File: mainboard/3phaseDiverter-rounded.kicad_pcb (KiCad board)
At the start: 2 copper layers, 133.8 x 119.3 mm, 138 parts, among them CN1 SMA, IC1 ATmega328-P, IC2 LM358, J0 FTDI, J1 RESET, J10 D10, J11 D11, J12 D12, J13 D13, J16 D2, J17 D3, J18 D4, J19 D5, J2 D2, J21 D6, J22 D7, J23 D8, J24 D9, J25 D10, J26 D11, J27 D12, J28 D13, J3 D3, J30 OLED, J31 DS18B20, J32 DS18B20, J4 D4, J5 D5, J6 D6, J7 D7, J8 D8, J9 D9, U1 AP2112R5-3.3TRG1, X1 16MHz

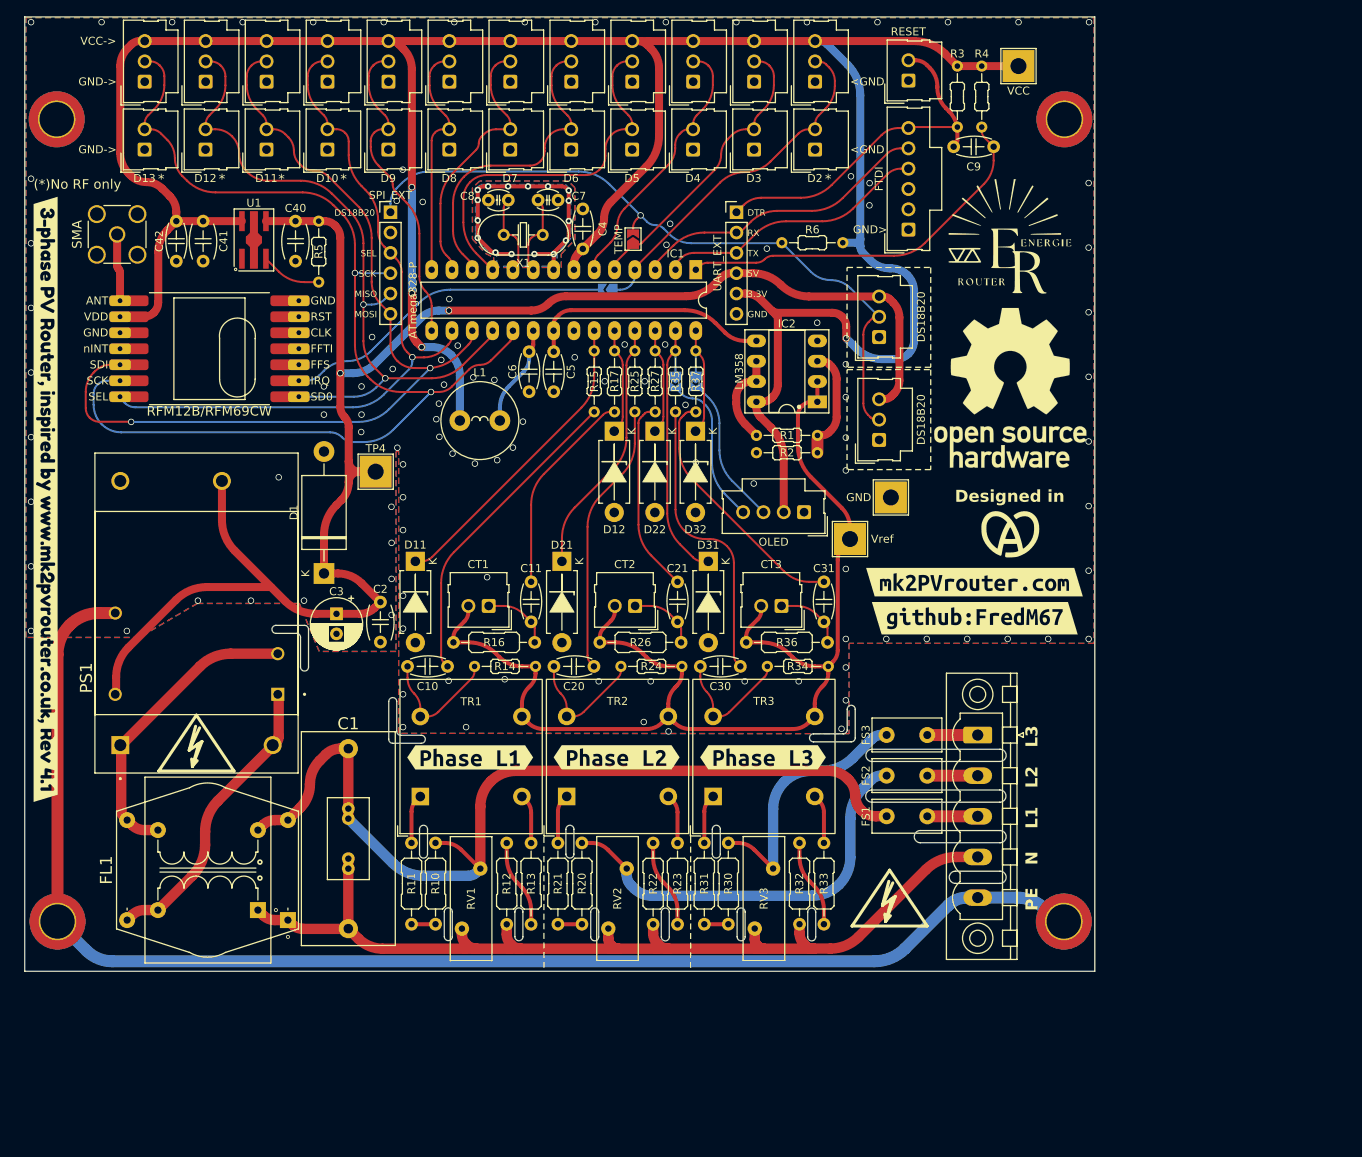
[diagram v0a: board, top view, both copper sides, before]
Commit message: Some SMD components
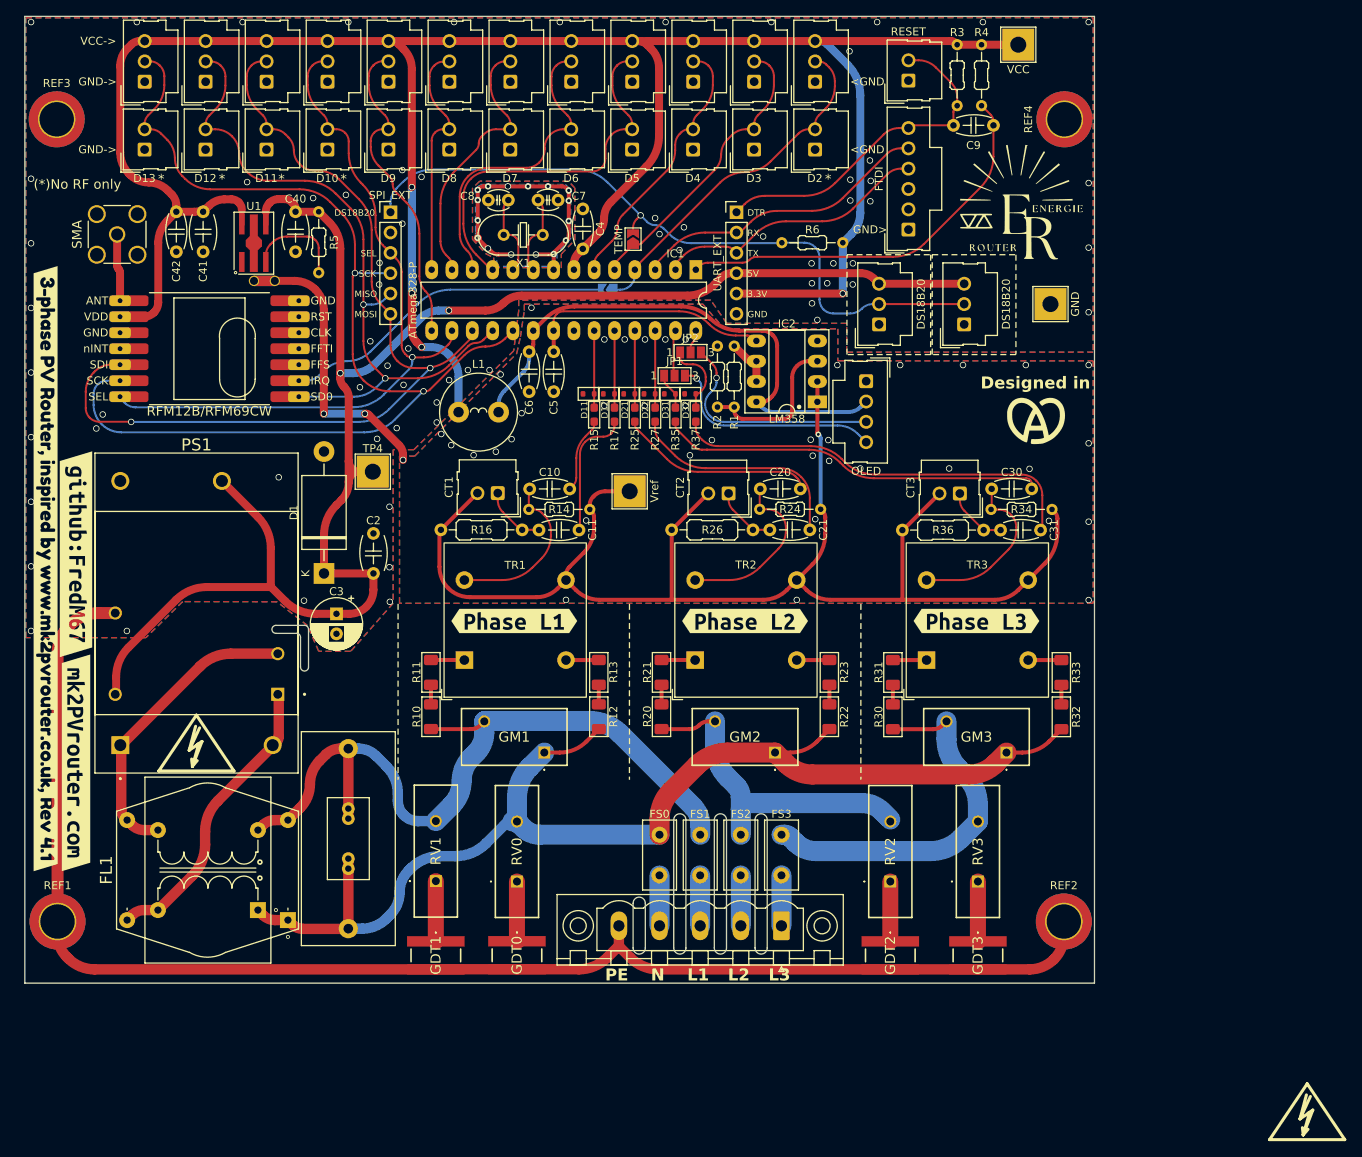
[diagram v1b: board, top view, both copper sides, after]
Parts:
- removed REF**: OSHW-Logo_19x20mm_SilkScreen, Symbol:OSHW-Logo_19x20mm_SilkScreen
- added FS0: 1A x 250V, Fuse:Fuse_Littelfuse_395Series, F.Cu at (92.6, 118.9)
- added GDT0: 2093-300-SM-RPLF, UserDef:2093300SMRPLF, F.Cu at (74.8, 134.0)
- added GDT1: 2093-300-SM-RPLF, UserDef:2093300SMRPLF, F.Cu at (64.6, 134.0)
- added GDT2: 2093-300-SM-RPLF, UserDef:2093300SMRPLF, F.Cu at (121.5, 134.0)
- added GDT3: 2093-300-SM-RPLF, UserDef:2093300SMRPLF, F.Cu at (132.4, 134.0)
- added GM1: 320V, UserDef:IsoM3300BL5, F.Cu at (78.2, 108.7)
- added GM2: 320V, UserDef:IsoM3300BL5, F.Cu at (107.0, 108.7)
- added GM3: 320V, UserDef:IsoM3300BL5, F.Cu at (136.0, 108.7)
- added NT0: NetTie_2, NetTie:NetTie-2_THT_Pad1.0mm, F.Cu at (41.9, 49.7)
- added RV0: 300V, UserDef:MOV14D471KKTR, F.Cu at (74.8, 124.8)
- D11, D12, D21, D22, D31, D32: value SA5.0A-TP -> UCLAMP3301H.TCT; footprint PCM_Diode_THT_AKL:D_DO-15_P10.16mm_Horizontal_Zener -> PCM_Diode_SMD_Handsoldering_AKL:D_SOD-523_TVS
- JP1, JP2: value SolderJumper_2_Open -> SolderJumper_3_Open; footprint Jumper:SolderJumper-2_P1.3mm_Open_TrianglePad1.0x1.5mm -> Jumper:SolderJumper-3_P1.3mm_Open_Pad1.0x1.5mm_NumberLabels; moved to F.Cu
- R10, R11, R12, R13, R20, R21, R22, R23, R30, R31, R32, R33: footprint PCM_Resistor_THT_AKL:R_Axial_DIN0207_L6.3mm_D2.5mm_P10.16mm_Horizontal -> PCM_Resistor_SMD_AKL:R_1206_3216Metric_Pad1.30x1.75mm_HandSolder
- R15, R17, R25, R27, R35, R37: footprint PCM_Resistor_THT_AKL:R_Axial_DIN0204_L3.6mm_D1.6mm_P7.62mm_Horizontal -> PCM_Resistor_SMD_AKL:R_0603_1608Metric_Pad1.05x0.95mm_HandSolder
- RV1, RV2, RV3: value Varistor -> 300V; footprint Varistor:RV_Disc_D15.5mm_W5.2mm_P7.5mm -> UserDef:MOV14D471KKTR
- moved kibuzzard-6431D11C-1 114.6 mm to (19.7, 110.0), turned to -90 degrees
- moved kibuzzard-64EB6544-1 112.6 mm to (19.7, 83.9), turned to -90 degrees
- moved REF13 81.3 mm to (25.1, 163.8)
- moved REF13 61.5 mm to (25.1, 156.0)
- moved REF10 58.6 mm to (173.6, 154.2)
- moved REF13 58.6 mm to (173.6, 154.2)
- moved R33 43.3 mm to (142.8, 98.7)
- moved C30 42.6 mm to (139.1, 75.7)
- moved R32 41.8 mm to (142.8, 104.2)
- moved R31 39.3 mm to (121.8, 98.7)
- moved R23 36.8 mm to (113.8, 98.6)
- moved RV2 35.7 mm to (121.5, 124.8)
- moved PWR1 34.2 mm to (107.8, 130.3), turned to 180 degrees
- moved R34 34.2 mm to (134.0, 78.3)
- moved R21 34.0 mm to (92.8, 98.6)
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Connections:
- C5 pad 1: GND -> AGND
- C6 pad 2: GND -> AGND
- D11 pad 2: GND -> AGND
- D12 pad 2: GND -> AGND
- D21 pad 2: GND -> AGND
- D22 pad 2: GND -> AGND
- D31 pad 1: A4 -> A4'
- D31 pad 2: GND -> AGND
- D32 pad 1: A5 -> A5'
- D32 pad 2: GND -> AGND
- IC1 pad 22: GND -> AGND
- IC2 pad 4: GND -> AGND
- IC2 pad 8: +3.3V -> AVCC
- J30 pad 1: GND -> AGND
- J30 pad 2: +3.3V -> AVCC
- JP1 pad 1: A4 -> A4'
- JP1 pad 2: Net-(J30-SDA) -> A4
- JP2 pad 1: A5 -> A5'
- JP2 pad 2: Net-(J30-SCL) -> A5
- PWR1 pad 4: NEUTRAL -> Net-(PWR1-N)
- R2 pad 2: GND -> AGND
- R35 pad 2: A4 -> A4'
- R37 pad 2: A5 -> A5'
- RV1 pad 1: NEUTRAL -> Net-(GDT1-Pad1)
- RV2 pad 1: NEUTRAL -> Net-(GDT2-Pad1)
- RV3 pad 1: NEUTRAL -> Net-(GDT3-Pad1)
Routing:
- net AVCC: track 12.6 -> 68.3 mm
- net +3.3V: track 351.2 -> 297.4 mm
- net AGND: track 0.00 -> 34.2 mm, vias 0 -> 41
- net Net-(C10-Pad1): track 39.8 -> 9.38 mm
- net A4: track 34.8 -> 5.35 mm
- net A0: track 38.6 -> 9.63 mm
- net VREF: track 149.4 -> 176.0 mm, vias 0 -> 1
- net A2: track 32.0 -> 9.63 mm
- net NEUTRAL: track 129.9 -> 152.3 mm
- net Net-(C31-Pad1): track 31.8 -> 52.0 mm
- net L1_VOLTAGE: track 116.1 -> 97.4 mm
- net L3_VOLTAGE: track 32.6 -> 47.1 mm
- net A5: track 16.3 -> 2.89 mm
- net Net-(C30-Pad1): track 36.5 -> 48.3 mm
- net GND: track 203.2 -> 213.9 mm, vias 128 -> 85
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- added copper zone on B.Cu, net AGND
- added copper zone on F.Cu, net AGND
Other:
- board size 133.8 x 119.3 mm -> 133.7 x 120.8 mm

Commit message: Add a lot of things !
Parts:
- removed kibuzzard-65568432: G005, kibuzzard-65568432
- added R0: 0R, PCM_Resistor_SMD_AKL:R_1206_3216Metric_Pad1.42x1.75mm_HandSolder, F.Cu at (17.4, 119.6)
- added REF10: Symbol_HighVoltage_Type2_Silk_VerySmall, Library:Symbol_HighVoltage_Type2_Silk_VerySmall, F.Cu at (84.1, 120.0)
- added kibuzzard-67FA4429: G***, kibuzzard-67FA4429, F.Cu at (15.6, 75.2)
- moved REF13 69.1 mm to (84.1, 120.0)
- moved REF10 47.1 mm to (141.3, 120.0)
- moved REF13 47.1 mm to (141.3, 120.0)
- moved kibuzzard-6431D11C-1 31.6 mm to (19.4, 78.4)
- moved kibuzzard-64EB6544-1 20.1 mm to (19.4, 104.0)
- moved CN1 3.54 mm to (22.4, 46.5)
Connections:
- GDT0 pad 2: GND -> Earth
- GDT1 pad 2: GND -> Earth
- GDT2 pad 2: GND -> Earth
- GDT3 pad 2: GND -> Earth
- PWR1 pad 5: GND -> Earth
- REF1 pad 1: GND -> Earth
- REF2 pad 1: GND -> Earth
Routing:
- net GND: track 213.9 -> 66.3 mm, vias 85 -> 86
- net Earth: track 0.00 -> 146.9 mm
- net L1_VOLTAGE: track 97.4 -> 100.4 mm, vias 0 -> 5
- net NEUTRAL: track 152.3 -> 154.5 mm, vias 0 -> 15
- net Net-(CN1-Pad1): track 8.38 -> 7.26 mm
- net Net-(C21-Pad1): track 28.5 -> 29.4 mm
- net AVCC: track 68.3 -> 69.1 mm
- net Net-(C30-Pad1): track 48.3 -> 47.7 mm
- net Net-(C20-Pad1): track 24.7 -> 24.0 mm
- net Net-(C31-Pad1): track 52.0 -> 52.7 mm
- net L3_VOLTAGE: track 47.1 -> 47.0 mm, vias 0 -> 5
- net L2_VOLTAGE: track 43.1 -> 43.2 mm, vias 0 -> 5
- net Net-(R33-Pad2): vias 0 -> 4
- net Net-(R32-Pad2): vias 0 -> 4
- net Net-(R31-Pad2): vias 0 -> 4
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- added copper zone on B.Cu, net L1_VOLTAGE
- added copper zone on F.Cu, net L1_VOLTAGE
- added copper zone on B.Cu, net L2_VOLTAGE
- added copper zone on F.Cu, net L2_VOLTAGE
- added copper zone on B.Cu, net L3_VOLTAGE
- added copper zone on F.Cu, net L3_VOLTAGE
- added copper zone on B.Cu, net NEUTRAL
- added copper zone on F.Cu, net NEUTRAL
- added copper zone on B.Cu, net Net-(R10-Pad2)
- added copper zone on F.Cu, net Net-(R10-Pad2)
- added copper zone on B.Cu, net Net-(R11-Pad2)
- added copper zone on F.Cu, net Net-(R11-Pad2)
- added copper zone on B.Cu, net Net-(R12-Pad2)
- added copper zone on F.Cu, net Net-(R12-Pad2)
- added copper zone on B.Cu, net Net-(R13-Pad2)
- added copper zone on F.Cu, net Net-(R13-Pad2)
- added copper zone on B.Cu, net Net-(R20-Pad2)
- added copper zone on F.Cu, net Net-(R20-Pad2)
- added copper zone on B.Cu, net Net-(R21-Pad2)
- added copper zone on F.Cu, net Net-(R21-Pad2)
- added copper zone on B.Cu, net Net-(R22-Pad2)
- added copper zone on F.Cu, net Net-(R22-Pad2)
- added copper zone on B.Cu, net Net-(R23-Pad2)
- added copper zone on F.Cu, net Net-(R23-Pad2)
- added copper zone on B.Cu, net Net-(R30-Pad2)
- added copper zone on F.Cu, net Net-(R30-Pad2)
- added copper zone on B.Cu, net Net-(R31-Pad2)
- added copper zone on F.Cu, net Net-(R31-Pad2)
- added copper zone on B.Cu, net Net-(R32-Pad2)
- added copper zone on F.Cu, net Net-(R32-Pad2)
- added copper zone on B.Cu, net Net-(R33-Pad2)
- added copper zone on F.Cu, net Net-(R33-Pad2)
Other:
- board text added: "EARTH to GND LINK"
